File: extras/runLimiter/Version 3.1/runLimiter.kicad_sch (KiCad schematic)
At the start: 15 parts, among them J1 5-20 Volts, J2 Vout, J3 Dry Contacts, K1 Relay, Q1 2N3904, Q2 2SD2023, U1 MCP1700-330, U2 ESP8266-01s

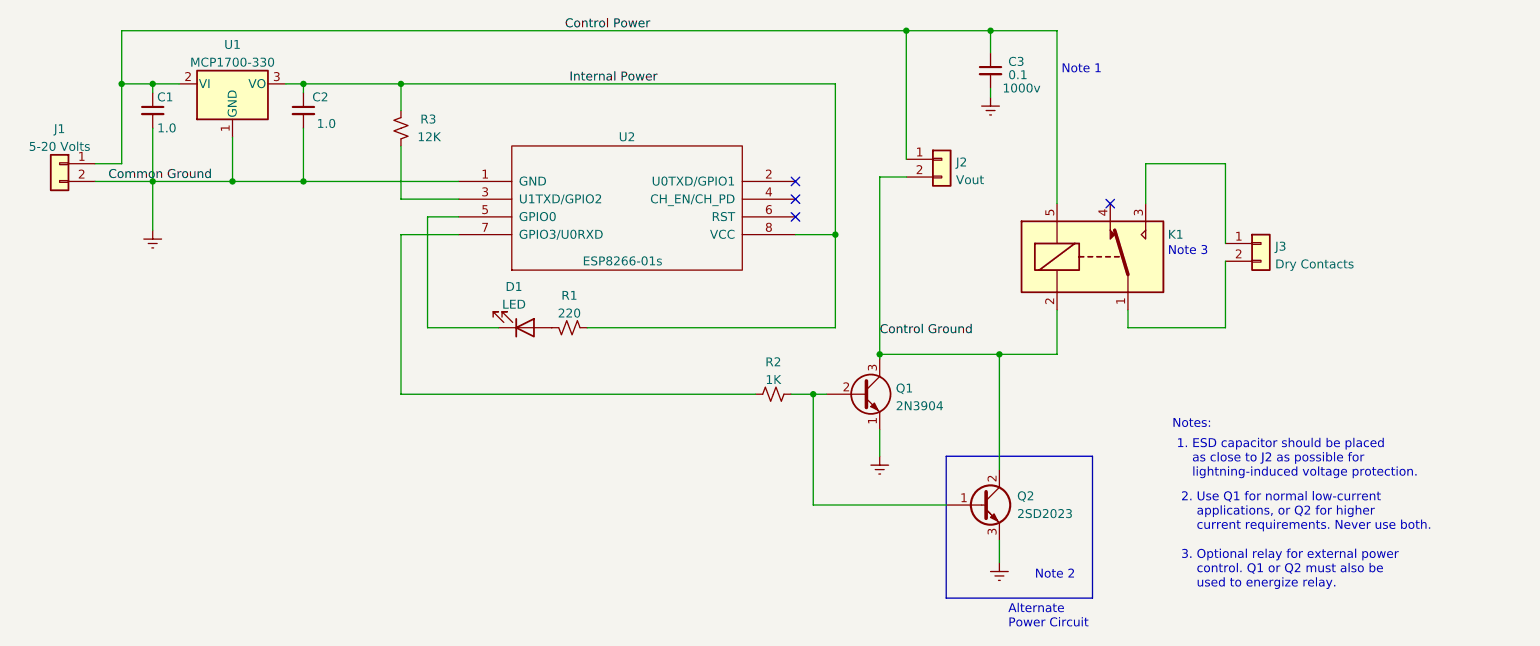
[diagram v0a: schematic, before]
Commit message: Changes to board and schematic
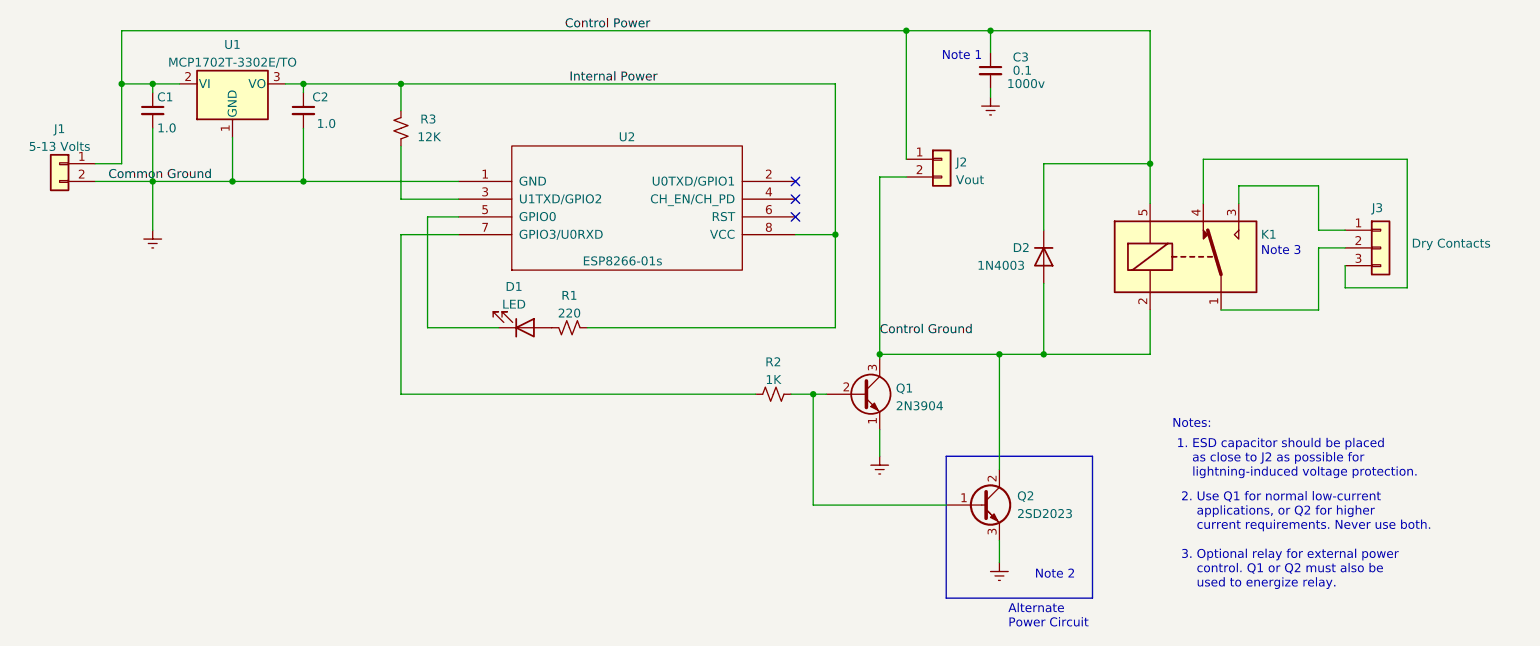
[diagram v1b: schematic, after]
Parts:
- removed J3: Dry Contacts, Connector_PinHeader_2.54mm:PinHeader_1x02_P2.54mm_Vertical, symbol Connector_TH_Headers:Conn_01x02
- added D2: 1N4003, Diode_THT:D_DO-41_SOD81_P10.16mm_Horizontal, symbol Diode:1N4003
- added J3: Dry Contacts, Connector_PinHeader_2.54mm:PinHeader_1x03_P2.54mm_Vertical, symbol Connector_Generic:Conn_01x03
- J1: value 5-20 Volts -> 5-13 Volts
- U1: value MCP1700-330 -> MCP1702T-3302E/TO
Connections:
- net Control Ground: now also D2.2 (A)
- net Control Power: now also D2.1 (K)
- net at K1.1: now also J3.2 (Pin_2)
- net at K1.3: now also J3.1 (Pin_1)
- net at K1.4: now also J3.3 (Pin_3)
- no-connect marks 4 -> 3
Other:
- moved on the sheet: K1
